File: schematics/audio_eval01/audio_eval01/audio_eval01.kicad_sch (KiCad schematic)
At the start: 2 parts, among them J1 Conn_01x08_Pin

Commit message: Audio evaluation board work.
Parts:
- added C1, C10, C12, C4, C6, C8: 0.1uF, Capacitor_SMD:C_0805_2012Metric_Pad1.18x1.45mm_HandSolder, symbol Device:C
- added C11, C9: 22uF, Capacitor_SMD:C_0805_2012Metric_Pad1.18x1.45mm_HandSolder, symbol Device:C
- added C13, C2, C3, C5, C7: 10uF, Capacitor_SMD:C_0805_2012Metric_Pad1.18x1.45mm_HandSolder, symbol Device:C
- added C25: 47uF, Capacitor_Tantalum_SMD:CP_EIA-3216-18_Kemet-A, symbol Device:C_Polarized
- added J2: AudioJack3, Connector_Audio:Jack_3.5mm_Switronic_ST-005-G_horizontal, symbol Connector_Audio:AudioJack3
- added J3: Conn_01x02_Pin, Connector_PinHeader_2.54mm:PinHeader_1x02_P2.54mm_Vertical, symbol Connector:Conn_01x02_Pin
- added R1, R3: R, Resistor_SMD:R_0805_2012Metric_Pad1.20x1.40mm_HandSolder, symbol Device:R
- added U2: AMS1117-1.8, Package_TO_SOT_SMD:SOT-223-3_TabPin2, symbol Regulator_Linear:AMS1117-1.8
- J1: value Conn_01x08_Pin -> Conn_01x10_Pin; footprint Connector_PinHeader_2.54mm:PinHeader_1x08_P2.54mm_Vertical -> Connector_PinHeader_2.54mm:PinHeader_1x10_P2.54mm_Vertical; symbol Connector:Conn_01x08_Pin -> Connector:Conn_01x10_Pin
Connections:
- net BCLK: now also J1.5 (Pin_5); no longer J1.2 (Pin_2)
- net GND: now also J1.1 (Pin_1), U1.13 (AIN1), U1.14 (AIN2), C1.2, C10.2, C11.2, C12.2, C13.2, C2.2, C25.2, C3.2, C4.2, C5.2, C6.2, C7.2, C8.2, C9.2, J2.S, U2.1 (GND)
- net GPIO1: now also J1.2 (Pin_2); no longer J1.8 (Pin_8)
- net MCLK: now also J1.6 (Pin_6); no longer J1.3 (Pin_3)
- net SCL: now also J1.8 (Pin_8), R3.2; no longer J1.5 (Pin_5)
- net SDA: now also J1.7 (Pin_7), R1.2; no longer J1.4 (Pin_4)
- net WCLK: now also J1.4 (Pin_4); no longer J1.1 (Pin_1)
- net 3V3: now reaches U1.17 (AVDD)
- net 3V3: now also J1.9 (Pin_9), U1.2 (IOVDD), U1.28 (HPVDD), C12.1, C13.1, C3.1, C4.1, C5.1, C6.1, C7.1, R1.1, R3.1, U2.3 (VI)
- net at U1.19 (SPKM): now also U1.23 (SPKM), J3.1 (Pin_1)
- net 5V0: now reaches U1.21 (SPKVDD)
- net 5V0: now also J1.10 (Pin_10), U1.24 (SPKVDD), C10.1, C11.1, C8.1, C9.1
- net at U1.22 (SPKP): now also U1.26 (SPKP), J3.2 (Pin_2)
- net at U1.27 (HPL): now also J2.T
- net 1V8: now reaches U1.3 (DVDD)
- net 1V8: now also C1.1, C2.1, C25.1, U2.2 (VO)
- net at U1.30 (HPR): now also J2.R
- net DIN: now reaches U1.5 (DIN)
- net DIN: now also J1.3 (Pin_3)
- no-connect marks 1 -> 2
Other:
- moved on the sheet: U1

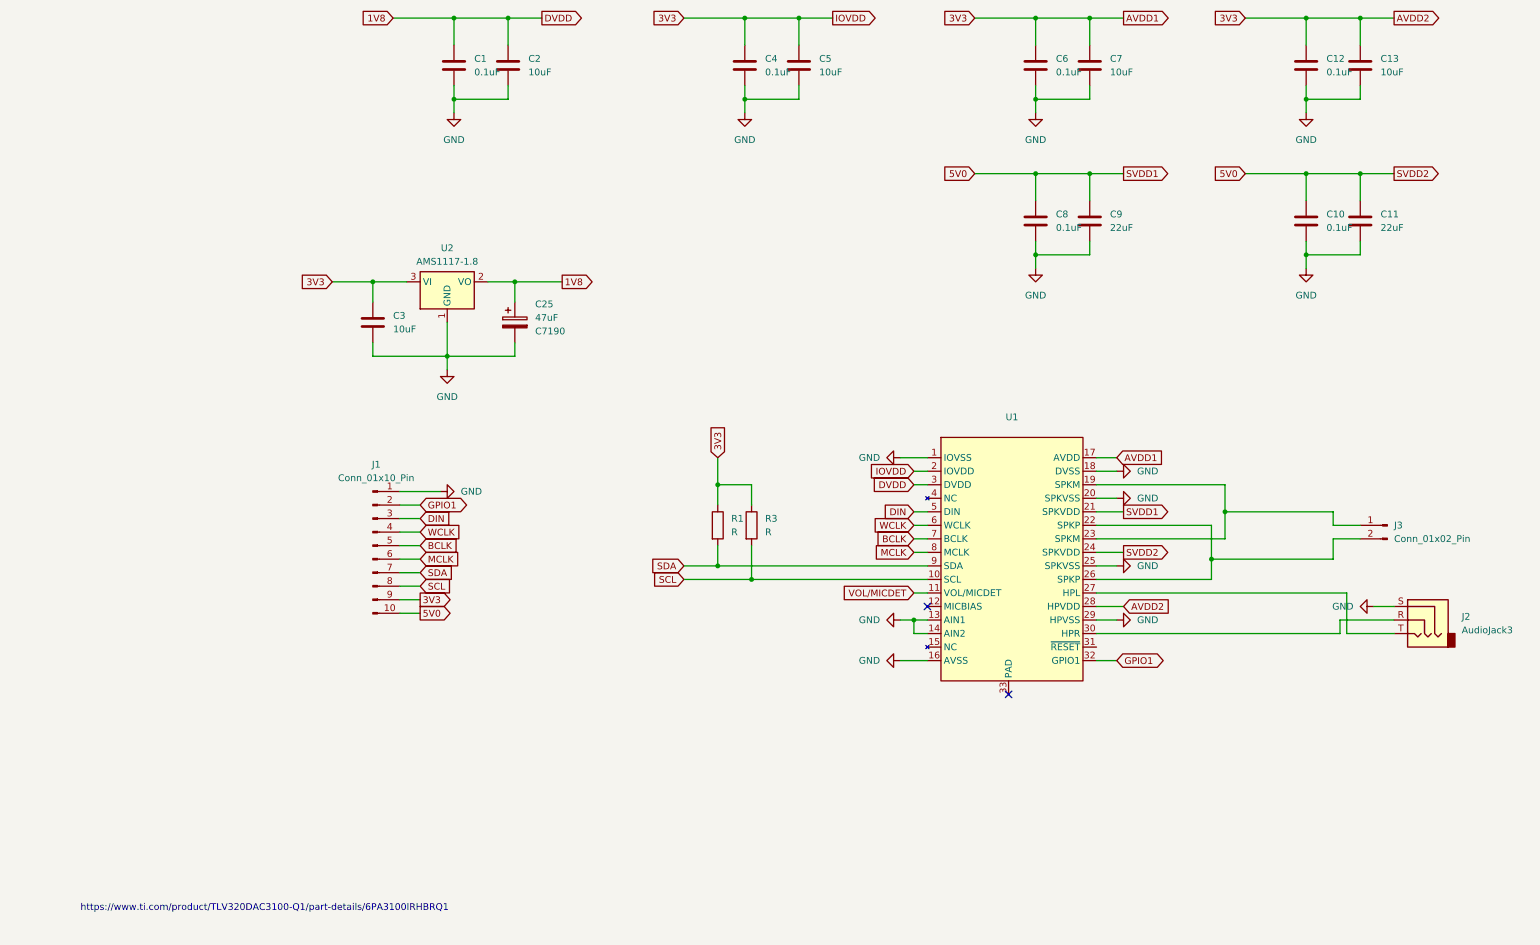
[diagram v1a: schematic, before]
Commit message: Minor DRC fixes to Audio evaluation board.
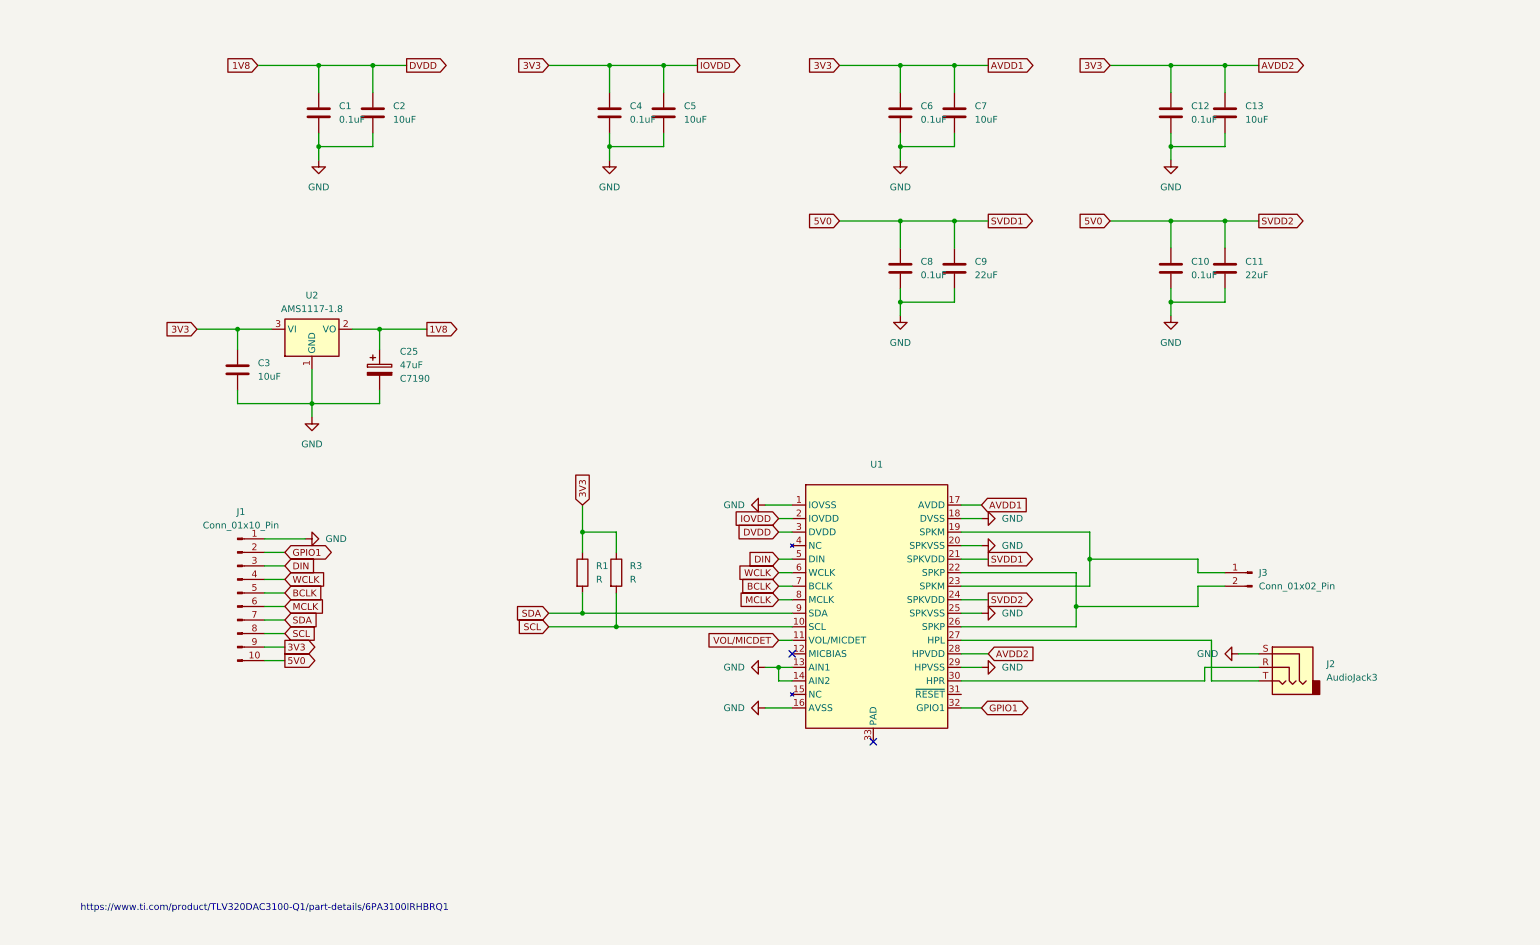
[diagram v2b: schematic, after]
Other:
- moved on the sheet: C1, C10, C11, C12, C13, C2, C25, C3, C4, C5, C6, C7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

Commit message: Prepared Audio evaluation board for manufacture.
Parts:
- C1, C10, C12, C4, C6, C8: LCSC (none) -> C28233
- C11, C9: LCSC (none) -> C15850
- C13, C2, C3, C5, C7: LCSC (none) -> C1713
- R1, R3: value R -> 4k7; LCSC (none) -> C17673
- U1: LCSC (none) -> C2667049
- U2: LCPC C6185 -> (none); LCSC (none) -> C6185
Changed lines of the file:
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@@
+			)
+		)
+		(property "LCSC" "C28233"
+			(at 226.06 68.58 0)
+			(effects
+				(font
+					(size 1.27 1.27)
+				)
 			)
 		)
@@
 			)
 		)
+		(property "LCSC" "C15850"
+			(at 236.22 68.58 0)
+			(effects
+				(font
+					(size 1.27 1.27)
+				)
+			)
+		)
 		(pin "2"
 		)
@@
 			)
 		)
+		(property "LCSC" "C1713"
+			(at 76.2 39.37 0)
+			(effects
+				(font
+					(size 1.27 1.27)
+				)
+			)
+		)
 		(pin "2"
 		)
@@
 			)
 		)
-		(property "Value" "R"
+		(property "Value" "4k7"
 			(at 124.46 126.9999 0)
 			(effects
@@
 			)
 		)
+		(property "LCSC" "C17673"
+			(at 121.92 125.73 0)
+			(effects
+				(font
+					(size 1.27 1.27)
+				)
+			)
+		)
 		(pin "2"
 		)
@@
 			)
 		)
+		(property "LCSC" "C28233"
+			(at 226.06 39.37 0)
+			(effects
+				(font
+					(size 1.27 1.27)
+				)
+			)
+		)
 		(pin "2"
 		)
@@
 			)
 		)
+		(property "LCSC" "C15850"
+			(at 185.42 68.58 0)
+			(effects
+				(font
+					(size 1.27 1.27)
+				)
+			)
+		)
 		(pin "2"
 		)
@@
 			)
 		)
+		(property "LCSC" "C1713"
+			(at 185.42 39.37 0)
+			(effects
+				(font
+					(size 1.27 1.27)
+				)
+			)
+		)
 		(pin "2"
 		)
@@
 			)
 		)
+		(property "LCSC" "C28233"
+			(at 120.65 39.37 0)
+			(effects
+				(font
+					(size 1.27 1.27)
+				)
+			)
+		)
 		(pin "2"
 		)
@@
 			)
 		)
+		(property "LCSC" "C28233"
+			(at 175.26 68.58 0)
+			(effects
+				(font
+					(size 1.27 1.27)
+				)
+			)
+		)
 		(pin "2"
 		)
@@
 			)
 		)
+		(property "LCSC" "C2667049"
+			(at 170.18 132.08 0)
+			(effects
+				(font
+					(size 1.27 1.27)
+				)
+			)
+		)
 		(pin "31"
 		)
@@
 			)
 		)
-		(property "Value" "R"
+		(property "Value" "4k7"
 			(at 118.11 126.9999 0)
 			(effects
@@
 				)
 				(hide yes)
+			)
+		)
+		(property "LCSC" "C17673"
+			(at 115.57 125.73 0)
+			(effects
+				(font
+					(size 1.27 1.27)
+				)
 			)
 		)
@@
 			)
 		)
+		(property "LCSC" "C1713"
+			(at 130.81 39.37 0)
+			(effects
+				(font
+					(size 1.27 1.27)
+				)
+				(hide yes)
+			)
+		)
 		(pin "2"
 		)
@@
 			)
 		)
+		(property "LCSC" "C1713"
+			(at 50.8 87.63 0)
+			(effects
+				(font
+					(size 1.27 1.27)
+				)
+			)
+		)
 		(pin "2"
 		)
@@
 			)
 		)
+		(property "LCSC" "C1713"
+			(at 236.22 39.37 0)
+			(effects
+				(font
+					(size 1.27 1.27)
+				)
+			)
+		)
 		(pin "2"
 		)
@@
 			)
 		)
+		(property "LCSC" "C28233"
+			(at 175.26 39.37 0)
+			(effects
+				(font
+					(size 1.27 1.27)
+				)
+			)
+		)
 		(pin "2"
 		)
@@
 			)
 		)
-		(property "LCPC" "C6185"
+		(property "LCSC" "C6185"
 			(at 64.77 80.01 0)
 			(effects
@@
 					(size 1.27 1.27)
 				)
-				(hide yes)
 			)
 		)
@@
 			)
 		)
+		(property "LCSC" "C28233"
+			(at 66.04 39.37 0)
+			(effects
+				(font
+					(size 1.27 1.27)
+				)
+			)
+		)

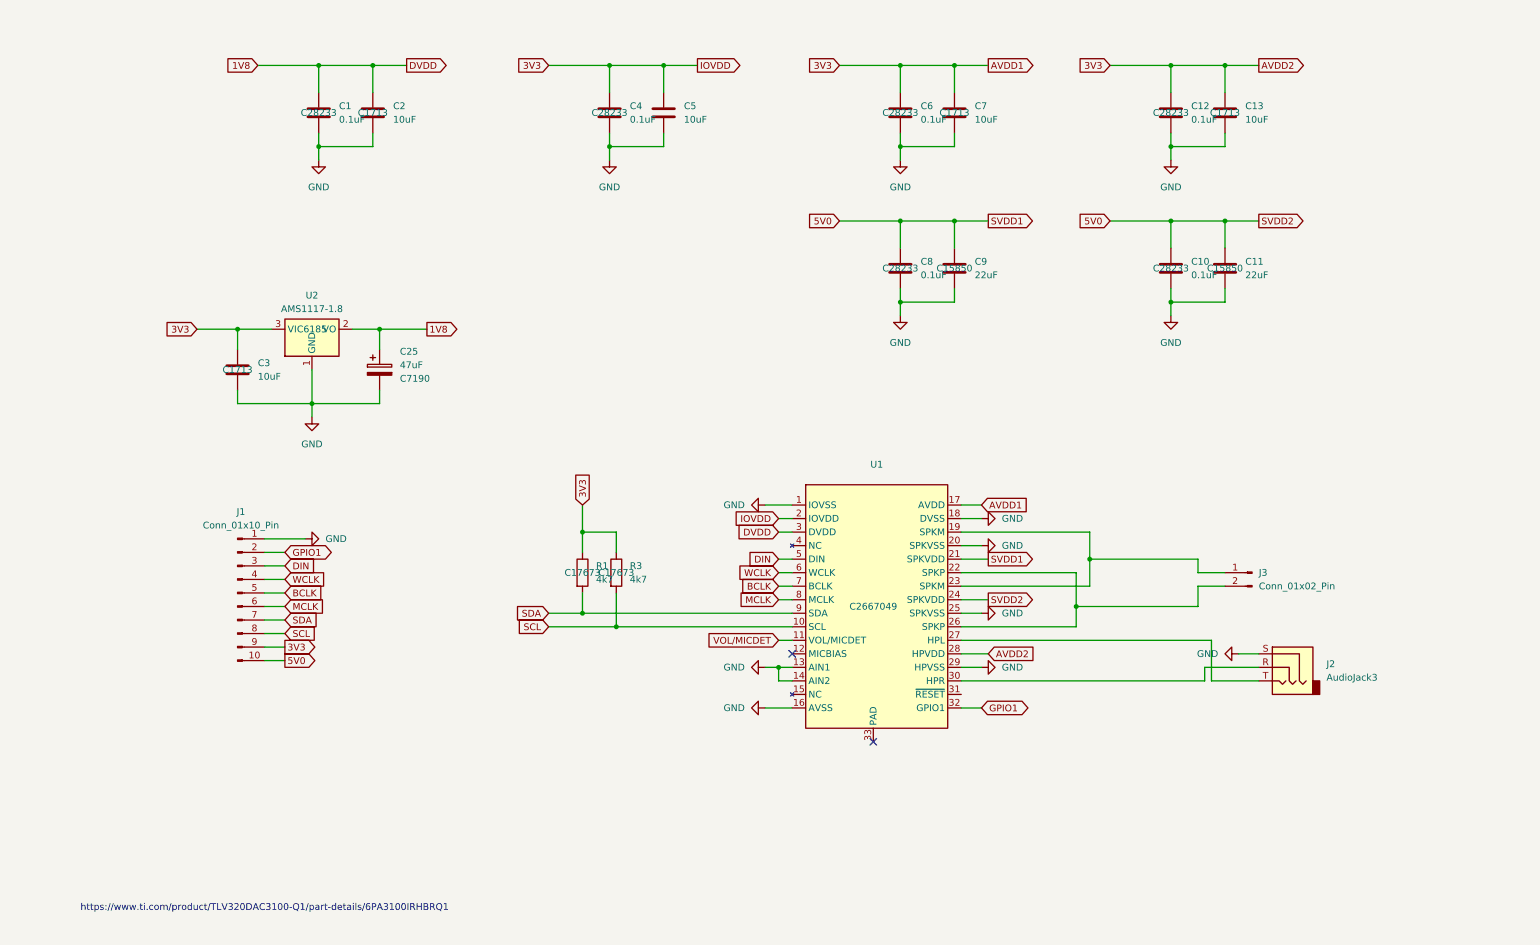
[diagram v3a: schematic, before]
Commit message: Reset circuit added to audio evaluation board.
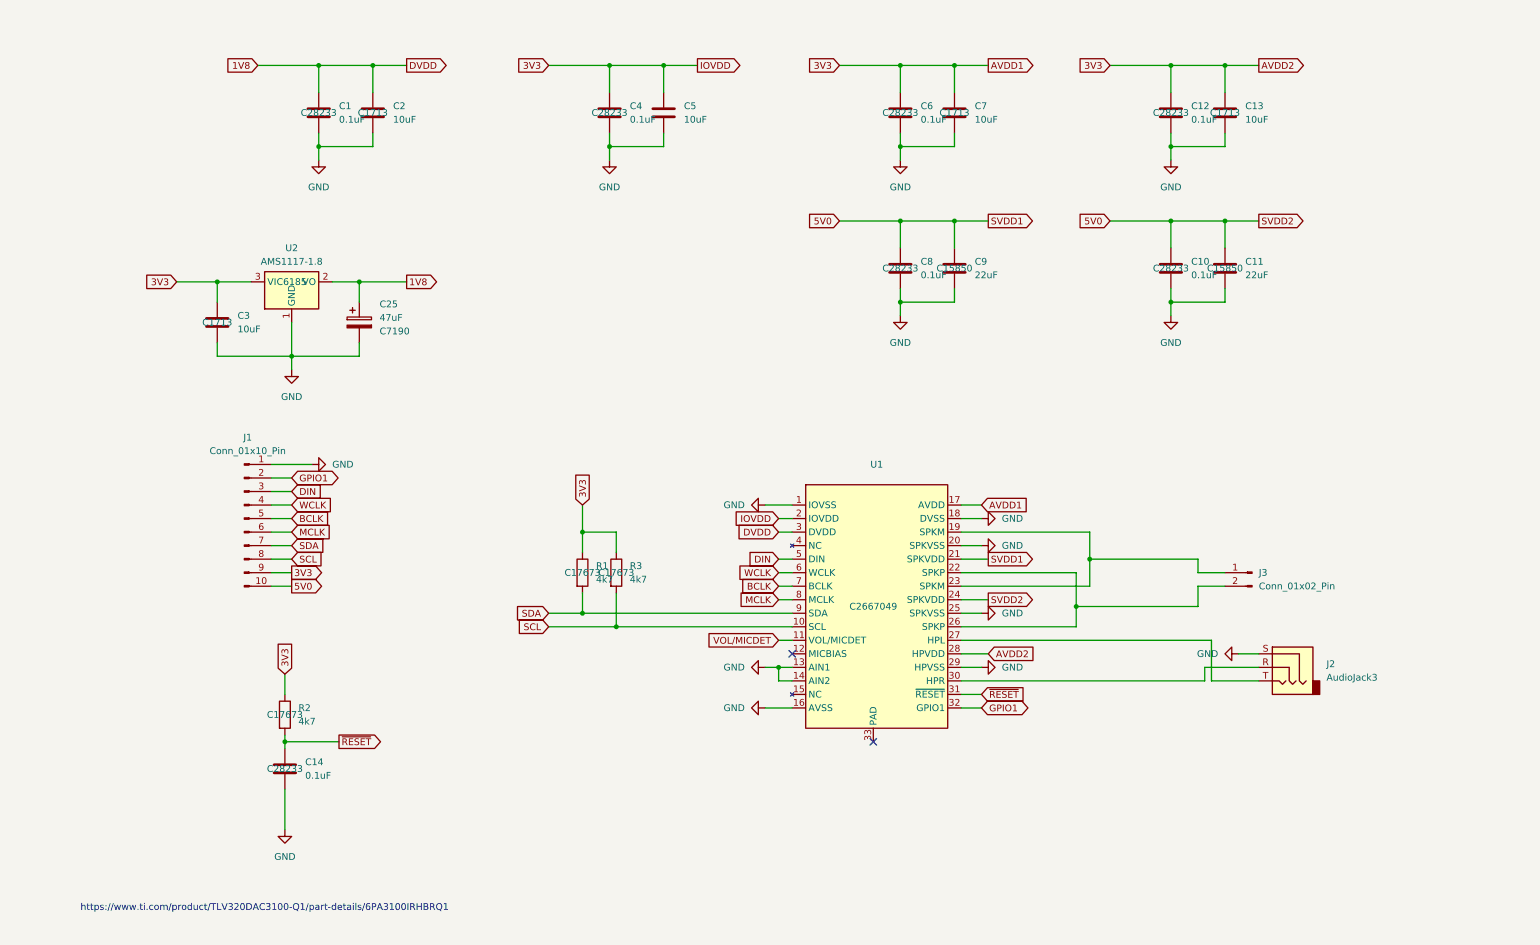
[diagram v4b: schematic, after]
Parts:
- added C14: 0.1uF, Capacitor_SMD:C_0805_2012Metric_Pad1.18x1.45mm_HandSolder, symbol Device:C
- added R2: 4k7, Resistor_SMD:R_0805_2012Metric_Pad1.20x1.40mm_HandSolder, symbol Device:R
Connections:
- net 3V3: now also R2.1
- net GND: now also C14.2
- net ~{RESET}: now reaches U1.31 (~{RESET})
- net ~{RESET}: now also C14.1, R2.2
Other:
- moved on the sheet: C25, C3, J1, U2

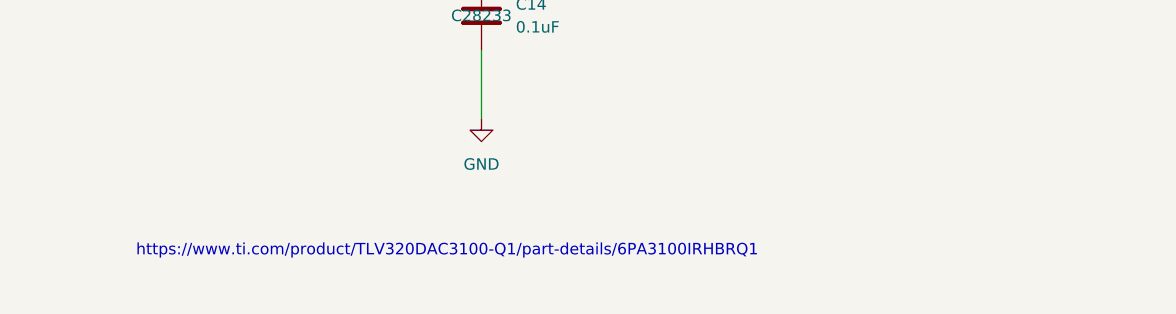
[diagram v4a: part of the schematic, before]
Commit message: Added a link to suitable audio jack for the audio eval board.
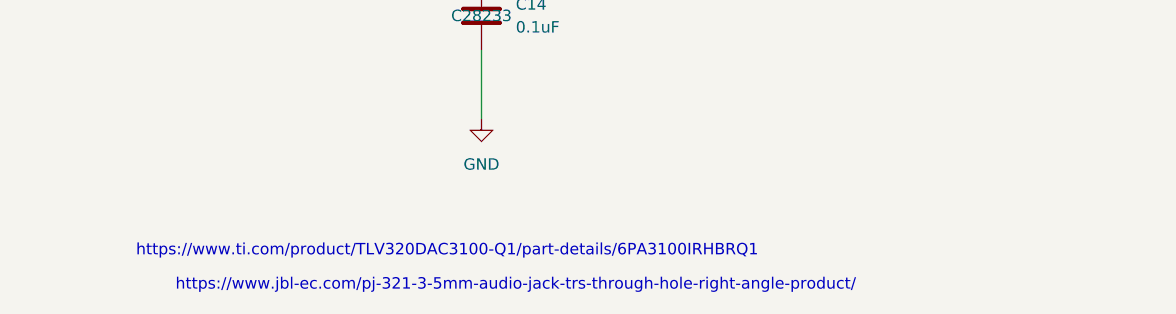
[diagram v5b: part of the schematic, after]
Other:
- note added: "https://www.jbl-ec.com/pj-321-3-5mm-audio-jack-trs-through-hole-right-angle-product/"
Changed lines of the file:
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@@
+		)
+	)
+	(text "https://www.jbl-ec.com/pj-321-3-5mm-audio-jack-trs-through-hole-right-angle-product/"
+		(exclude_from_sim no)
+		(at 63.5 192.532 0)
+		(effects
+			(font
+				(size 1.27 1.27)
+			)
+			(href "https://www.jbl-ec.com/pj-321-3-5mm-audio-jack-trs-through-hole-right-angle-product/")
 		)
 	)
